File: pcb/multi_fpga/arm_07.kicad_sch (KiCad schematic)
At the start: 16 parts, among them U57 IM72D128V01XTMA1, U58 IM72D128V01XTMA1, U59 IM72D128V01XTMA1, U60 IM72D128V01XTMA1, U61 IM72D128V01XTMA1, U62 IM72D128V01XTMA1, U63 IM72D128V01XTMA1, U64 IM72D128V01XTMA1

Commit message: Fixed library and power issues.
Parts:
- C57, C58, C59, C60, C61, C62, C63, C64: symbol C -> multi_fpga:C
- U57, U58, U59, U60, U61, U62, U63, U64: symbol IM72D128 -> multi_fpga:IM72D128

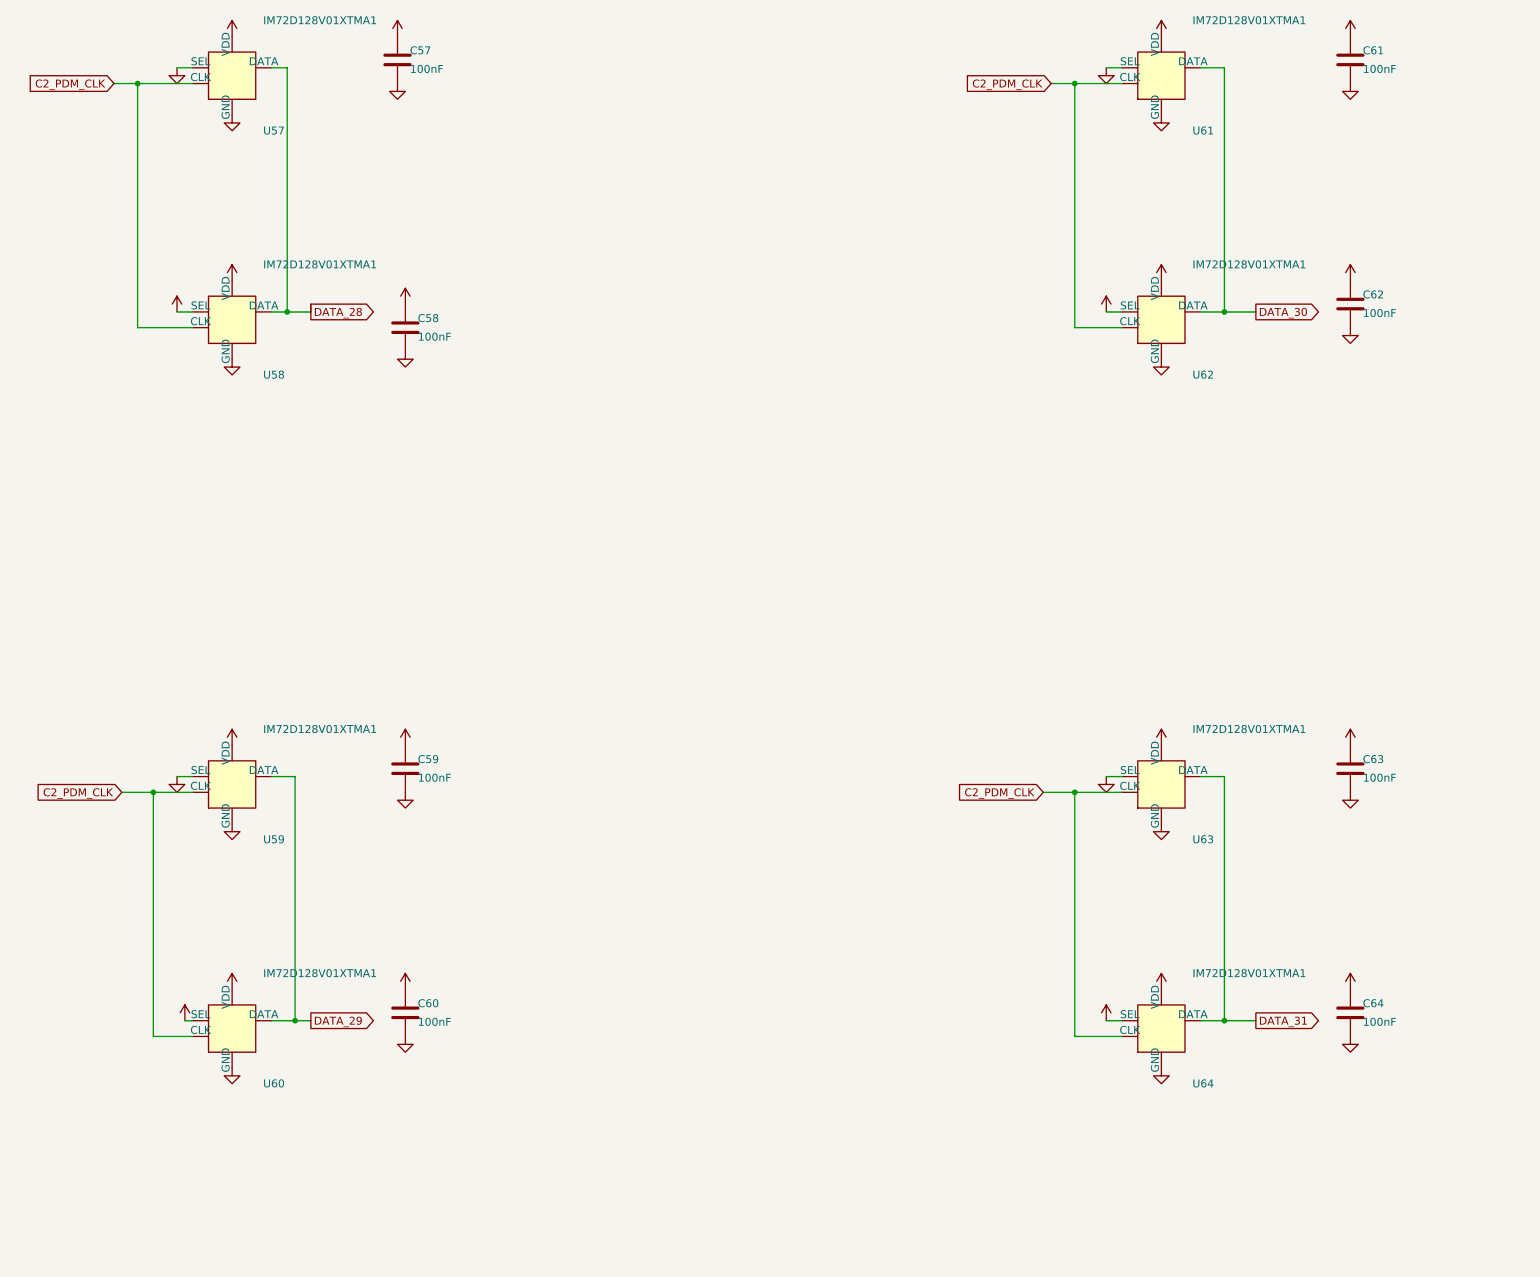
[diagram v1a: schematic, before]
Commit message: Fixed power and C ref des collisions.
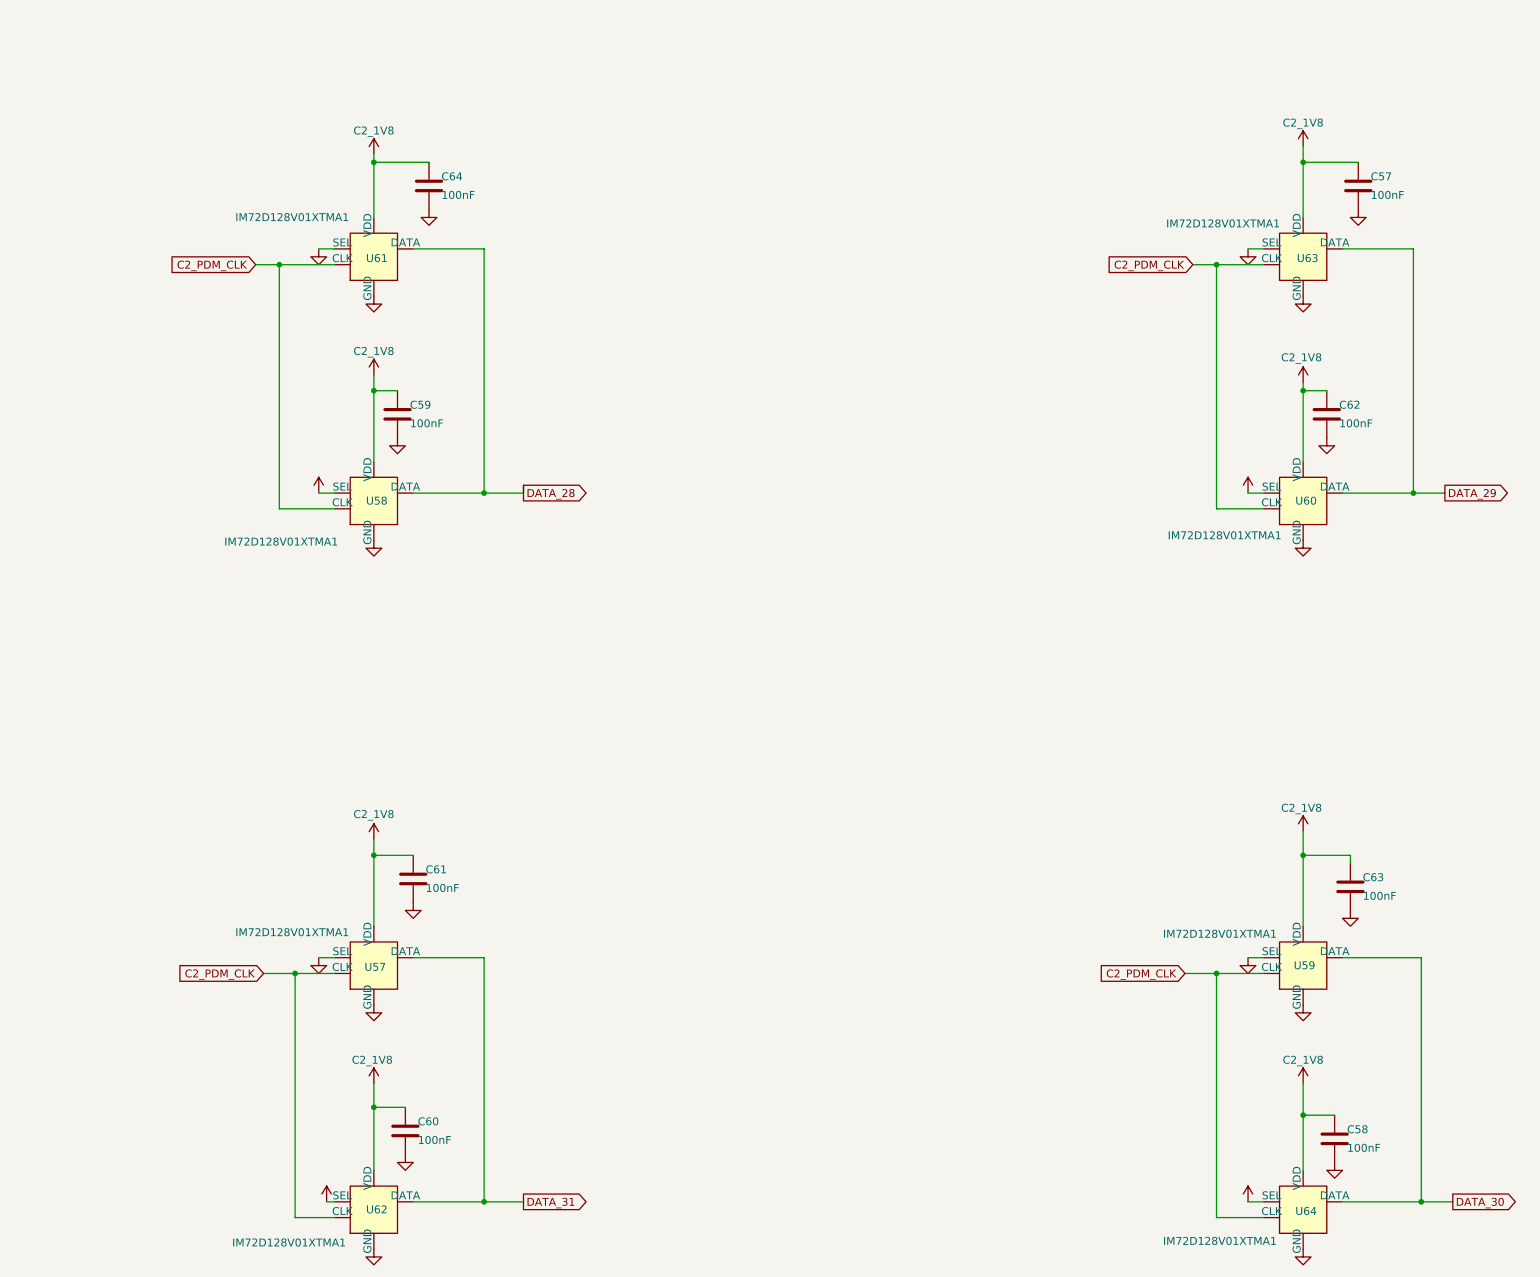
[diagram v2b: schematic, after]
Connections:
- net DATA_28: now also U61.1 (DATA); no longer U57.1 (DATA)
- net DATA_29: now also U63.1 (DATA); no longer U59.1 (DATA)
- net DATA_30: now also U59.1 (DATA), U64.1 (DATA); no longer U61.1 (DATA), U62.1 (DATA)
- net DATA_31: now also U57.1 (DATA), U62.1 (DATA); no longer U63.1 (DATA), U64.1 (DATA)

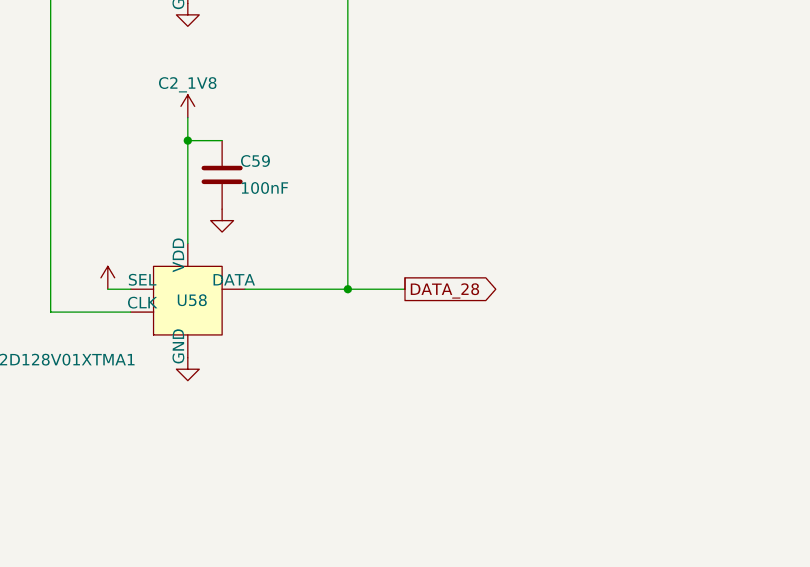
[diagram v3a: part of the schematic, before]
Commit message: Fixed regulator connection errors and dangling wire.
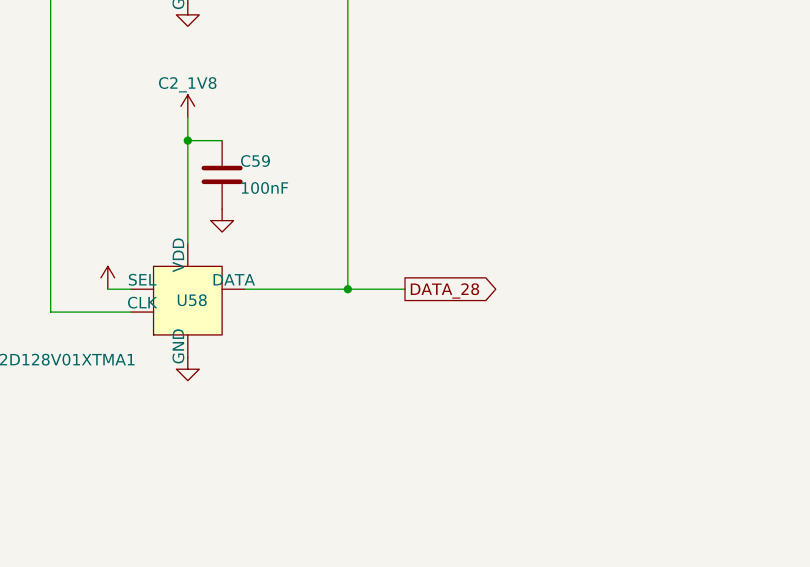
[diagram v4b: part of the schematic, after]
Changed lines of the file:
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@@
-	(wire
-		(pts
-			(xy 127 106.68) (xy 127 107.95)
-		)
-		(stroke
-			(width 0)
-			(type default)
-		)
-	)
 	(wire
 		(pts

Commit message: Global fix of res defs.
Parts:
- renumbered C59 to C74, C60 to C75, C61 to C76, C64 to C77, C62 to C78, C58 to C79, C63 to C80, C57 to C81, U61 to U57, U57 to U59, U62 to U60, U63 to U61, U60 to U62, U59 to U63

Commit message: Changed to use generic cap symbols and footprints.
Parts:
- C74, C75, C76, C77, C78, C79, C80, C81: symbol multi_fpga:C -> Device:C
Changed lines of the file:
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@@
 	)
 	(symbol
-		(lib_id "multi_fpga:C")
+		(lib_id "Device:C")
 		(at 256.54 95.25 0)
 		(unit 1)
@@
 		)
 		(property "Footprint" ""
-			(at 256.54 95.25 0)
+			(at 257.5052 99.06 0)
 			(hide yes)
 			(show_name no)
@@
 			)
 		)
-		(property "Description" ""
+		(property "Description" "Unpolarized capacitor"
 			(at 256.54 95.25 0)
 			(hide yes)
@@
 	)
 	(symbol
-		(lib_id "multi_fpga:C")
+		(lib_id "Device:C")
 		(at 261.62 58.42 0)
 		(unit 1)
@@
 		)
 		(property "Footprint" ""
-			(at 261.62 58.42 0)
+			(at 262.5852 62.23 0)
 			(hide yes)
 			(show_name no)
@@
 			)
 		)
-		(property "Description" ""
+		(property "Description" "Unpolarized capacitor"
 			(at 261.62 58.42 0)
 			(hide yes)
@@
 	)
 	(symbol
-		(lib_id "multi_fpga:C")
+		(lib_id "Device:C")
 		(at 111.76 58.42 0)
 		(unit 1)
@@
 		)
 		(property "Footprint" ""
-			(at 111.76 58.42 0)
+			(at 112.7252 62.23 0)
 			(hide yes)
 			(show_name no)
@@
 			)
 		)
-		(property "Description" ""
+		(property "Description" "Unpolarized capacitor"
 			(at 111.76 58.42 0)
 			(hide yes)
@@
 	)
 	(symbol
-		(lib_id "multi_fpga:C")
+		(lib_id "Device:C")
 		(at 257.81 212.09 0)
 		(unit 1)
@@
 		)
 		(property "Footprint" ""
-			(at 257.81 212.09 0)
+			(at 258.7752 215.9 0)
 			(hide yes)
 			(show_name no)
@@
 			)
 		)
-		(property "Description" ""
+		(property "Description" "Unpolarized capacitor"
 			(at 257.81 212.09 0)
 			(hide yes)
@@
 	)
 	(symbol
-		(lib_id "multi_fpga:C")
+		(lib_id "Device:C")
 		(at 260.35 171.45 0)
 		(unit 1)
@@
 		)
 		(property "Footprint" ""
-			(at 260.35 171.45 0)
+			(at 261.3152 175.26 0)
 			(hide yes)
 			(show_name no)
@@
 			)
 		)
-		(property "Description" ""
+		(property "Description" "Unpolarized capacitor"
 			(at 260.35 171.45 0)
 			(hide yes)
@@
 	)
 	(symbol
-		(lib_id "multi_fpga:C")
+		(lib_id "Device:C")
 		(at 106.68 95.25 0)
 		(unit 1)
@@
 		)
 		(property "Footprint" ""
-			(at 106.68 95.25 0)
+			(at 107.6452 99.06 0)
 			(hide yes)
 			(show_name no)
@@
 			)
 		)
-		(property "Description" ""
+		(property "Description" "Unpolarized capacitor"
 			(at 106.68 95.25 0)
 			(hide yes)
@@
 	)
 	(symbol
-		(lib_id "multi_fpga:C")
+		(lib_id "Device:C")
 		(at 107.95 210.82 0)
 		(unit 1)
@@
 		)
 		(property "Footprint" ""
-			(at 107.95 210.82 0)
+			(at 108.9152 214.63 0)
 			(hide yes)
 			(show_name no)
@@
 			)
 		)
-		(property "Description" ""
+		(property "Description" "Unpolarized capacitor"
 			(at 107.95 210.82 0)
 			(hide yes)
@@
 	)
 	(symbol
-		(lib_id "multi_fpga:C")
+		(lib_id "Device:C")
 		(at 109.22 170.18 0)
 		(unit 1)
@@
 		)
 		(property "Footprint" ""
-			(at 109.22 170.18 0)
+			(at 110.1852 173.99 0)
 			(hide yes)
 			(show_name no)
@@
 			)
 		)
-		(property "Description" ""
+		(property "Description" "Unpolarized capacitor"
 			(at 109.22 170.18 0)
 			(hide yes)

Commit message: Added stock footprints for C symbols.
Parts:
- C74, C75, C76, C77, C78, C79, C80, C81: footprint (none) -> Capacitor_SMD:C_0603_1608Metric
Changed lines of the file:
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@@
 			)
 		)
-		(property "Footprint" ""
+		(property "Footprint" "Capacitor_SMD:C_0603_1608Metric"
 			(at 257.5052 99.06 0)
 			(hide yes)
@@
 			)
 		)
-		(property "Footprint" ""
+		(property "Footprint" "Capacitor_SMD:C_0603_1608Metric"
 			(at 262.5852 62.23 0)
 			(hide yes)
@@
 			)
 		)
-		(property "Footprint" ""
+		(property "Footprint" "Capacitor_SMD:C_0603_1608Metric"
 			(at 112.7252 62.23 0)
 			(hide yes)
@@
 			)
 		)
-		(property "Footprint" ""
+		(property "Footprint" "Capacitor_SMD:C_0603_1608Metric"
 			(at 258.7752 215.9 0)
 			(hide yes)
@@
 			)
 		)
-		(property "Footprint" ""
+		(property "Footprint" "Capacitor_SMD:C_0603_1608Metric"
 			(at 261.3152 175.26 0)
 			(hide yes)
@@
 			)
 		)
-		(property "Footprint" ""
+		(property "Footprint" "Capacitor_SMD:C_0603_1608Metric"
 			(at 107.6452 99.06 0)
 			(hide yes)
@@
 			)
 		)
-		(property "Footprint" ""
+		(property "Footprint" "Capacitor_SMD:C_0603_1608Metric"
 			(at 108.9152 214.63 0)
 			(hide yes)
@@
 			)
 		)
-		(property "Footprint" ""
+		(property "Footprint" "Capacitor_SMD:C_0603_1608Metric"
 			(at 110.1852 173.99 0)
 			(hide yes)
